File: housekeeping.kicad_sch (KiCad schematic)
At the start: 54 parts, among them U1 MC34063A, U2 MC34063A, U3 MC34063A, U4 MC34063A

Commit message: Changed fill types for SW nets and added silkscreen labels for banana connectors
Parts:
- R15, R16, R5, R7, R8, R9: footprint Resistor_SMD:R_0201_0603Metric_Pad0.64x0.40mm_HandSolder -> Resistor_SMD:R_0603_1608Metric_Pad0.98x0.95mm_HandSolder
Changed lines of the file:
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@@
 			)
 		)
-		(property "Footprint" "Resistor_SMD:R_0201_0603Metric_Pad0.64x0.40mm_HandSolder"
+		(property "Footprint" "Resistor_SMD:R_0603_1608Metric_Pad0.98x0.95mm_HandSolder"
 			(at 59.69 83.82 0)
 			(effects
@@
 			)
 		)
-		(property "Footprint" "Resistor_SMD:R_0201_0603Metric_Pad0.64x0.40mm_HandSolder"
+		(property "Footprint" "Resistor_SMD:R_0603_1608Metric_Pad0.98x0.95mm_HandSolder"
 			(at 100.33 104.14 0)
 			(effects
@@
 			)
 		)
-		(property "Footprint" "Resistor_SMD:R_0201_0603Metric_Pad0.64x0.40mm_HandSolder"
+		(property "Footprint" "Resistor_SMD:R_0603_1608Metric_Pad0.98x0.95mm_HandSolder"
 			(at 92.71 184.15 0)
 			(effects
@@
 			)
 		)
-		(property "Footprint" "Resistor_SMD:R_0201_0603Metric_Pad0.64x0.40mm_HandSolder"
+		(property "Footprint" "Resistor_SMD:R_0603_1608Metric_Pad0.98x0.95mm_HandSolder"
 			(at 224.79 184.15 0)
 			(effects
@@
 			)
 		)
-		(property "Footprint" "Resistor_SMD:R_0201_0603Metric_Pad0.64x0.40mm_HandSolder"
+		(property "Footprint" "Resistor_SMD:R_0603_1608Metric_Pad0.98x0.95mm_HandSolder"
 			(at 71.12 109.22 0)
 			(effects
@@
 			)
 		)
-		(property "Footprint" "Resistor_SMD:R_0201_0603Metric_Pad0.64x0.40mm_HandSolder"
+		(property "Footprint" "Resistor_SMD:R_0603_1608Metric_Pad0.98x0.95mm_HandSolder"
 			(at 223.52 107.95 0)
 			(effects

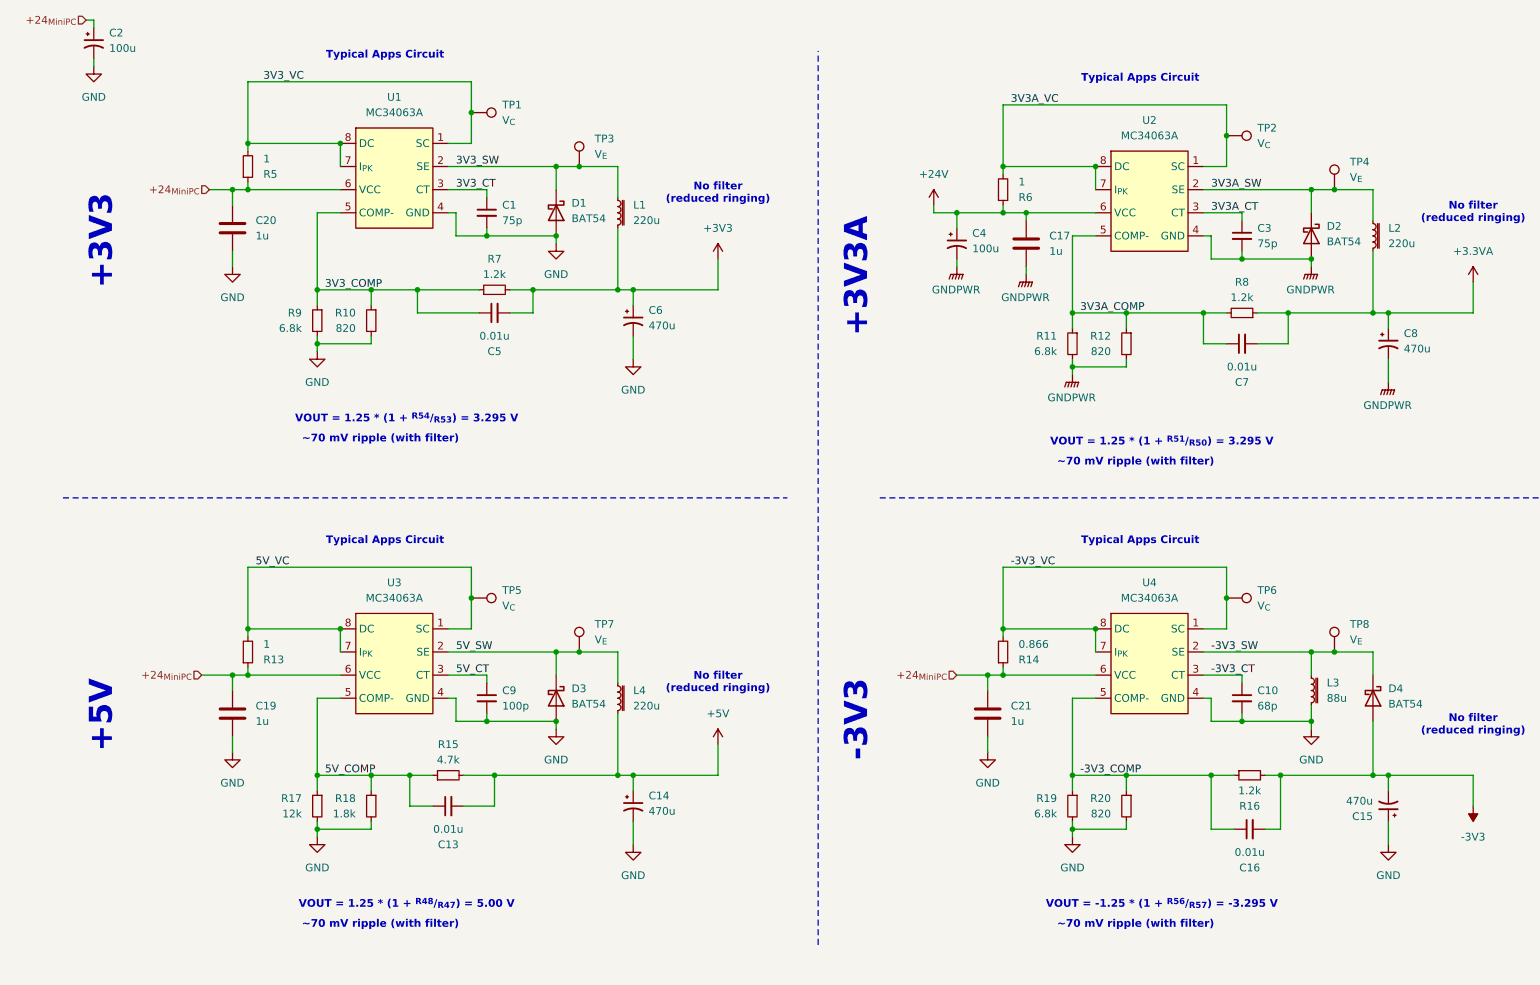
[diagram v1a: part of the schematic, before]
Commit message: Completed stage 2 schematic
+ added SPICE models for all the custom components
+ renumbered components
+ updated library with stage 2 symbols
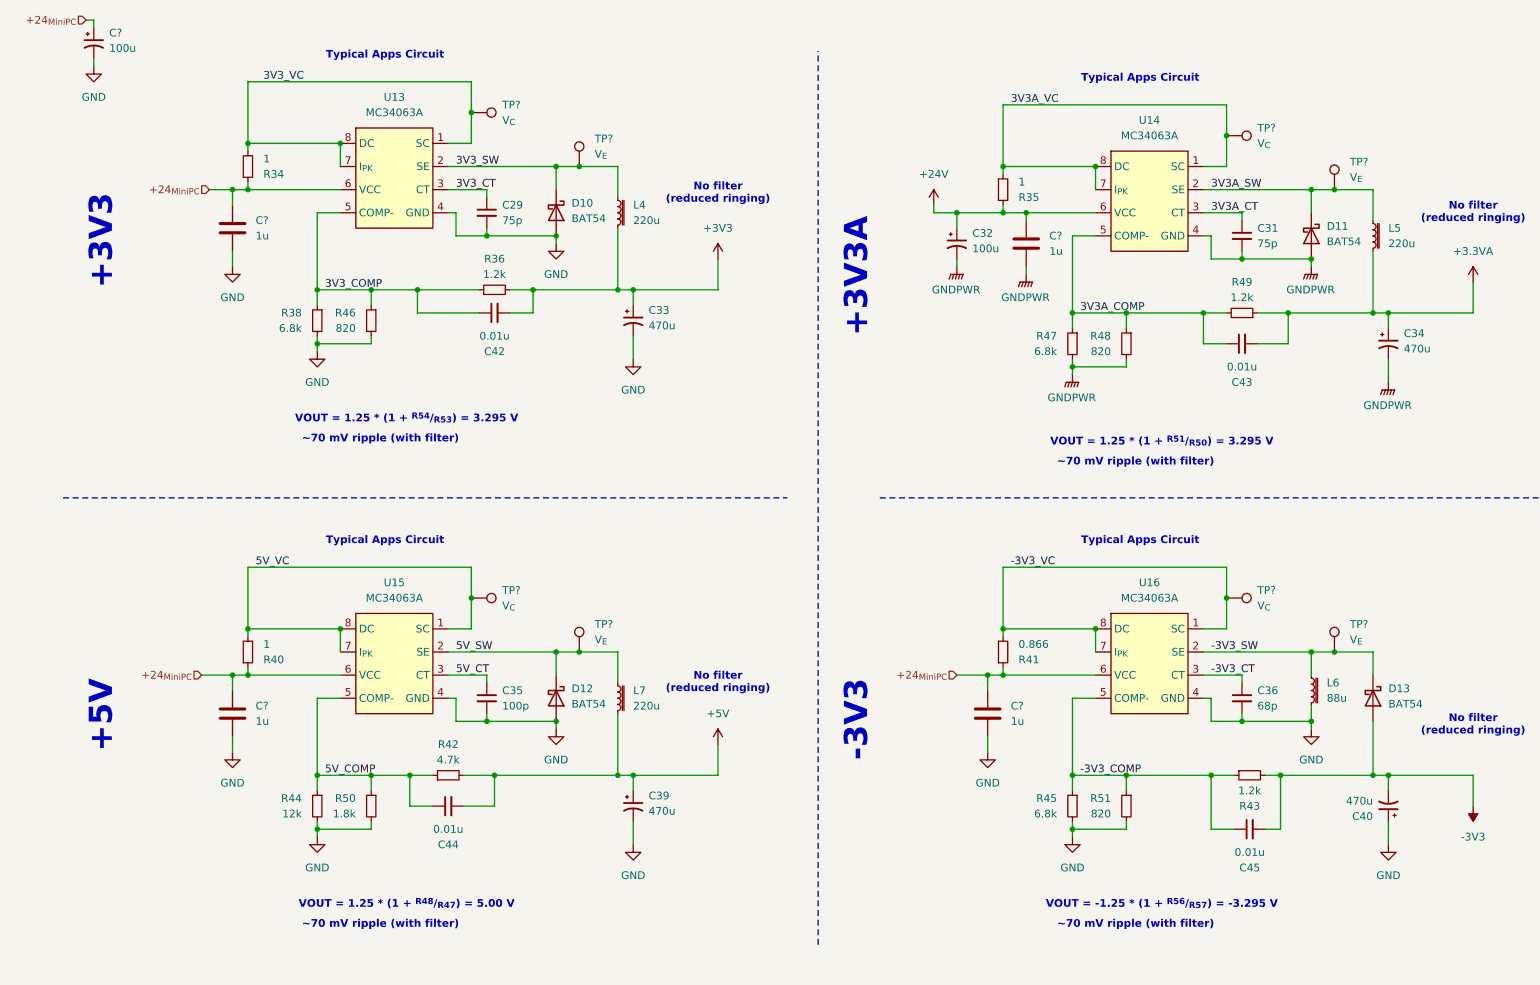
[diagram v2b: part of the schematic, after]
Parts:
- renumbered C1 to C29, C3 to C31, C4 to C32, C6 to C33, C8 to C34, C9 to C35, C10 to C36, C14 to C39, C15 to C40, C5 to C42, C7 to C43, C13 to C44, C16 to C45, C19 to C?, C17 to C?, C2 to C?, C21 to C?, C20 to C?, D1 to D10, D2 to D11, D3 to D12, D4 to D13, L1 to L4, L2 to L5, L3 to L6, L4 to L7, R5 to R34, R6 to R35, R7 to R36, R9 to R38, R13 to R40, R14 to R41, R15 to R42, R16 to R43, R17 to R44, R19 to R45, R10 to R46, R11 to R47, R12 to R48, R8 to R49, R18 to R50, R20 to R51, TP5 to TP?, TP8 to TP?, TP4 to TP?, TP1 to TP?, TP2 to TP?, TP7 to TP?, TP6 to TP?, TP3 to TP?, U1 to U13, U2 to U14, U3 to U15, U4 to U16

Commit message: Redesign housekeeping supplies
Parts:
- removed C31: 75p, Capacitor_SMD:C_0603_1608Metric_Pad1.08x0.95mm_HandSolder, symbol Device:C_Small
- removed C32: 100u, Capacitor_THT:CP_Radial_D8.0mm_P3.50mm, symbol Device:C_Polarized_Small_US
- removed C36: 68p, Capacitor_SMD:C_0603_1608Metric_Pad1.08x0.95mm_HandSolder, symbol Device:C_Small
- removed C40: 470u, Capacitor_THT:CP_Radial_D6.3mm_P2.50mm, symbol Device:C_Polarized_Small_US
- removed C45: 0.01u, Capacitor_SMD:C_0603_1608Metric_Pad1.08x0.95mm_HandSolder, symbol Device:C_Small
- removed C? (x2): 1u, Capacitor_SMD:C_0603_1608Metric_Pad1.08x0.95mm_HandSolder, symbol Device:C
- removed D13: BAT54, Package_TO_SOT_SMD:SOT-23_Handsoldering, symbol Device:D_Schottky
- removed L6: 88u, ! Robomaster Passives:ASPIAIGS6055221MT, symbol Device:L_Iron_Small
- removed R35: 1, Resistor_SMD:R_0603_1608Metric_Pad0.98x0.95mm_HandSolder, symbol Device:R_Small
- removed R48, R51: 820, Resistor_SMD:R_0603_1608Metric_Pad0.98x0.95mm_HandSolder, symbol Device:R_Small
- removed R49: 1.2k, Resistor_SMD:R_0603_1608Metric_Pad0.98x0.95mm_HandSolder, symbol Device:R_Small
- removed TP? (x2): V_{E}, TestPoint:TestPoint_Bridge_Pitch2.0mm_Drill0.7mm, symbol Connector:TestPoint
- removed TP? (x2): V_{C}, TestPoint:TestPoint_Bridge_Pitch2.0mm_Drill0.7mm, symbol Connector:TestPoint
- removed U14: MC34063A, Package_SO:SOIC-8_3.9x4.9mm_P1.27mm, symbol ! Robomaster ICs:MC34063A
- added C31: 1u, Capacitor_SMD:C_0603_1608Metric_Pad1.08x0.95mm_HandSolder, symbol Device:C
- added C32: 100p, Capacitor_SMD:C_0603_1608Metric_Pad1.08x0.95mm_HandSolder, symbol Device:C_Small
- C33, C34, C39: footprint Capacitor_THT:CP_Radial_D6.3mm_P2.50mm -> Capacitor_THT:CP_Radial_D10.0mm_P5.00mm; Mouser Part Number 710-860010273011 -> 710-860020575014
- R34: value 1 -> 1.5k
- R38: value 6.8k -> 180k
- R41: value 0.866 -> 0.75; footprint Resistor_SMD:R_0805_2012Metric_Pad1.20x1.40mm_HandSolder -> Resistor_SMD:R_0603_1608Metric_Pad0.98x0.95mm_HandSolder; Mouser Part Number 603-RL0603JR-070R24L -> 603-RL1206FR-070R75L
- R43: value 1.2k -> 1k
- R45, R47: value 6.8k -> 22k
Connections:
- net -3V3 is gone; now on net GND: R43.2
- net -3V3_COMP is gone; now on net 3V3_COMP: R43.1, R45.1, U16.5 (COMP-)
- net -3V3_CT is gone; now on net 3V3_CT: U16.3 (CT)
- net -3V3_SW is gone; now on net GND: U16.2 (SE)
- net 3V3A_COMP is gone; now on net 3V3_COMP: C43.1, R47.1
- net +24_{MiniPC}: now also C31.1
- net 3V3_CT: now also C32.1
- net GND: now also C34.2, R47.2, C31.2, C32.2; no longer R45.2
- net +3.3VA renamed VCC
- net VCC: now also D11.3 (K), R45.2; no longer L5.2
- net -3V3_VC renamed 30V_VC
- net 30V_VC: now also L5.1; no longer U16.1 (SC)
- removed net 3V3A_SW: D11.3 (K), L5.1
- removed net GNDPWR: C34.2, D11.1 (A), R47.2
- new net 30V_SW: D11.1 (A), L5.2, U16.1 (SC)
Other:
- note added: "+30V"
- note added: "Input power filtering"
- note removed: "+3V3A"
- note removed: "-3V3"
- note removed: "Typical Apps Circuit"
- note removed: "VOUT = -1.25 * (1 + ^{R56}/_{R57}) = -3.295 V"
- note removed: "VOUT = 1.25 * (1 + ^{R51}/_{R50}) = 3.295 V"
- moved on the sheet: C?, D10, D12

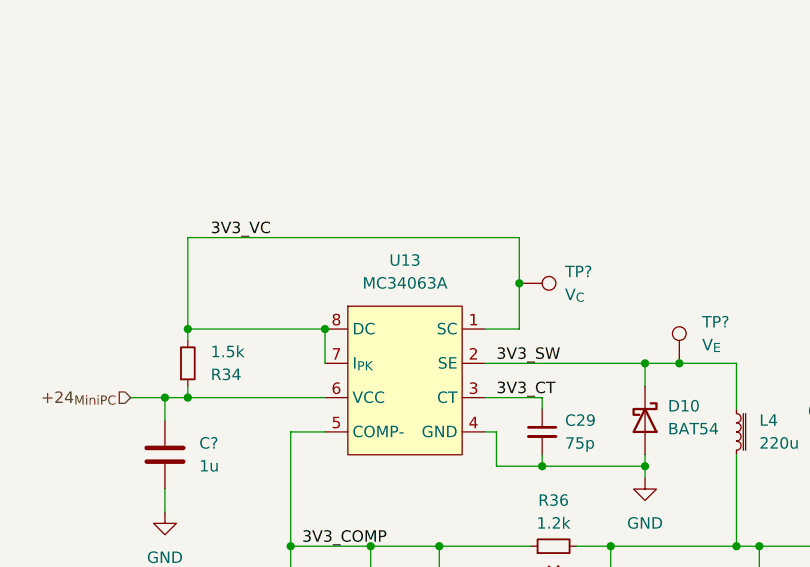
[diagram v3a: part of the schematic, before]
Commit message: Update Mouser part numbers
Some resistors will be wrong, please check
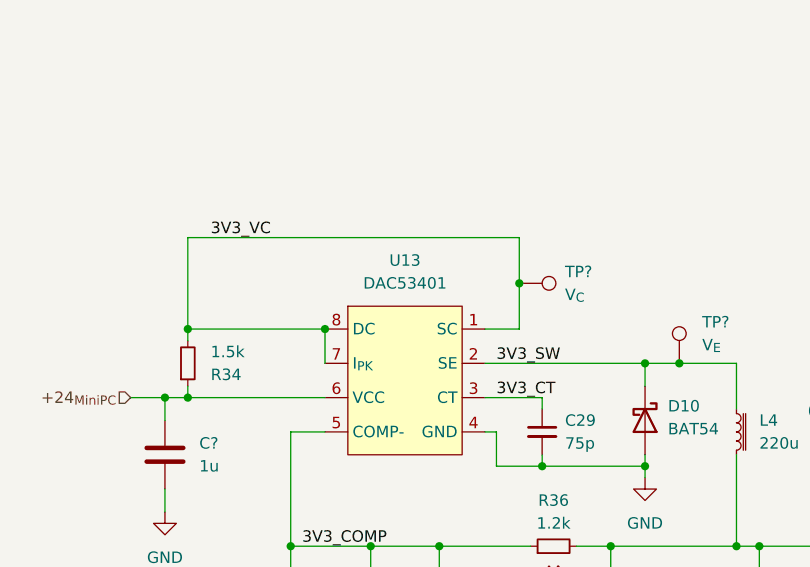
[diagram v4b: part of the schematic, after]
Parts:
- R34: Mouser Part Number 667-ERJ-3RQFR33V -> (none)
- R38, R46, R47: Mouser Part Number 755-ESR03EZPJ222 -> (none)
- R45: Mouser Part Number 603-RT0603FRE133K6L -> (none)
- U13: value MC34063A -> DAC53401; footprint Package_SO:SOIC-8_3.9x4.9mm_P1.27mm -> Package_SON:WSON-8-1EP_2x2mm_P0.5mm_EP0.9x1.6mm; Mouser Part Number 595-MC34063ADR -> 595-DAC53401DSGR
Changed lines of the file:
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@@
 			)
 		)
-		(property "Value" "MC34063A"
+		(property "Value" "DAC53401"
 			(at 83.82 74.93 0)
 			(effects
@@
 			)
 		)
-		(property "Footprint" "Package_SO:SOIC-8_3.9x4.9mm_P1.27mm"
+		(property "Footprint" "Package_SON:WSON-8-1EP_2x2mm_P0.5mm_EP0.9x1.6mm"
 			(at 83.82 77.47 0)
 			(effects
@@
 			)
 		)
-		(property "Mouser Part Number" "595-MC34063ADR"
+		(property "Mouser Part Number" "595-DAC53401DSGR"
 			(at 83.82 77.47 0)
 			(effects
@@
 			)
 		)
-		(property "Mouser Part Number" "667-ERJ-3RQFR33V"
+		(property "Mouser Part Number" ""
 			(at 59.69 83.82 0)
 			(effects
@@
 			)
 		)
-		(property "Mouser Part Number" "603-RT0603FRE133K6L"
+		(property "Mouser Part Number" ""
 			(at 231.14 104.14 0)
 			(effects
@@
 			)
 		)
-		(property "Mouser Part Number" "755-ESR03EZPJ222"
+		(property "Mouser Part Number" ""
 			(at 80.01 109.22 0)
 			(effects
@@
 			)
 		)
-		(property "Mouser Part Number" "755-ESR03EZPJ222"
+		(property "Mouser Part Number" ""
 			(at 210.82 109.22 0)
 			(effects
@@
 			)
 		)
-		(property "Mouser Part Number" "755-ESR03EZPJ222"
+		(property "Mouser Part Number" ""
 			(at 71.12 109.22 0)
 			(effects
